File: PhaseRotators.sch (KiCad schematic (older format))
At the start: 7 parts, among them U2 74LVC1G00DCKR, U4 74LVC1G00DCKR, U8 74LCX574

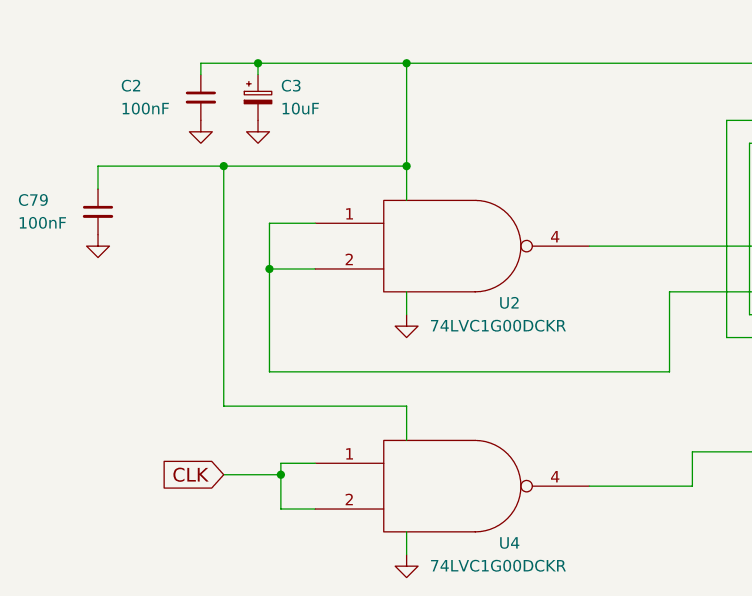
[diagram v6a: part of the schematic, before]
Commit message: PCB 74LCX574
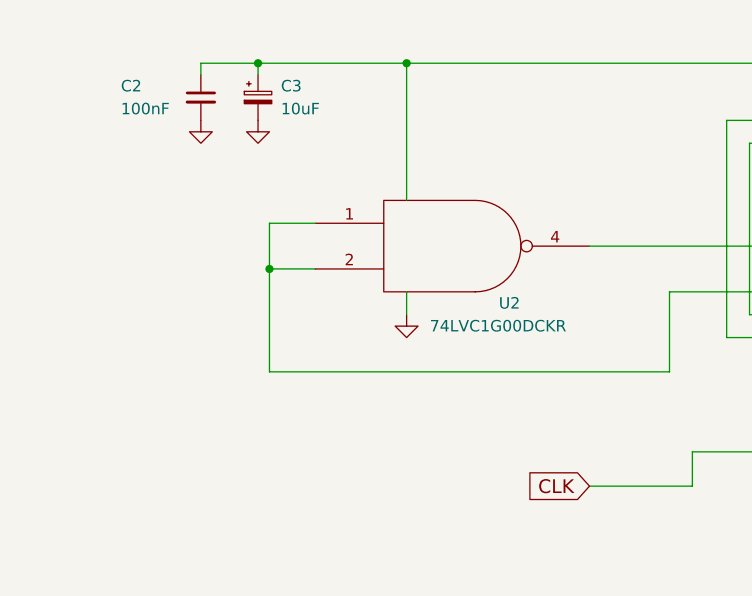
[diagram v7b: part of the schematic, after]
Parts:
- removed C79: 100nF, UI:C_1206_0603, symbol C_Small
- removed U4: 74LVC1G00DCKR, TO_SOT_Packages_SMD:SOT-353_SC-70-5, symbol 74LVC1G00DCKR
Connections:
- net CLK: now also U8.11 (Cp)
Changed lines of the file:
@@
 Comment4 ""
 $EndDescr
-Text GLabel 3600 3700 0    60   Input ~ 0
+Text GLabel 5200 3750 0    60   Input ~ 0
 CLK
 $Comp
@@
 $EndComp
 $Comp
-L GND #PWR43
+L GND #PWR42
 U 1 1 5EAC7395
 P 3750 2150
-F 0 "#PWR43" H 3750 1900 50  0001 C CNN
+F 0 "#PWR42" H 3750 1900 50  0001 C CNN
 F 1 "GND" H 3750 2000 50  0001 C CNN
 F 2 "" H 3750 2150 50  0001 C CNN
@@
 $EndComp
 $Comp
-L GND #PWR42
+L GND #PWR41
 U 1 1 5EAC76D0
 P 3500 2150
-F 0 "#PWR42" H 3500 1900 50  0001 C CNN
+F 0 "#PWR41" H 3500 1900 50  0001 C CNN
 F 1 "GND" H 3500 2000 50  0001 C CNN
 F 2 "" H 3500 2150 50  0001 C CNN
@@
 	6900 1900 6900 2650
 $Comp
-L GND #PWR46
+L GND #PWR44
 U 1 1 5ED0A7D2
 P 6900 3900
-F 0 "#PWR46" H 6900 3650 50  0001 C CNN
+F 0 "#PWR44" H 6900 3650 50  0001 C CNN
 F 1 "GND" H 6900 3750 50  0001 C CNN
 F 2 "" H 6900 3900 50  0001 C CNN
@@
 	4400 2900 4400 3000
 $Comp
-L GND #PWR44
+L GND #PWR43
 U 1 1 5ED0ABB8
 P 4400 3000
-F 0 "#PWR44" H 4400 2750 50  0001 C CNN
+F 0 "#PWR43" H 4400 2750 50  0001 C CNN
 F 1 "GND" H 4400 2850 50  0001 C CNN
 F 2 "" H 4400 3000 50  0001 C CNN
@@
 Wire Wire Line
 	5650 3600 6200 3600
-Wire Wire Line
-	3600 3700 3850 3700
-Wire Wire Line
-	3850 3650 3850 3850
-Wire Wire Line
-	3850 3650 4000 3650
-Wire Wire Line
-	3850 3850 4000 3850
-Connection ~ 3850 3700
 Connection ~ 4400 1900
 $Comp
@@
 	1    0    0    -1
 $EndComp
-$Comp
-L 74LVC1G00DCKR U4
-U 1 1 5ED1F8EE
-P 4600 3750
-F 0 "U4" H 4850 3500 50  0000 C CNN
-F 1 "74LVC1G00DCKR" H 4800 3400 50  0000 C CNN
-F 2 "TO_SOT_Packages_SMD:SOT-353_SC-70-5" H 4600 3750 50  0001 C CNN
-F 3 "" H 4600 3750 50  0001 C CNN
-	1    4600 3750
-	1    0    0    -1
-$EndComp
-Wire Wire Line
-	3050 2350 4400 2350
-Wire Wire Line
-	3600 3400 4400 3400
-Wire Wire Line
-	4400 3400 4400 3550
-Connection ~ 4400 2350
-$Comp
-L GND #PWR45
-U 1 1 5ED1F9E3
-P 4400 4050
-F 0 "#PWR45" H 4400 3800 50  0001 C CNN
-F 1 "GND" H 4400 3900 50  0001 C CNN
-F 2 "" H 4400 4050 50  0001 C CNN
-F 3 "" H 4400 4050 50  0001 C CNN
-	1    4400 4050
-	1    0    0    -1
-$EndComp
-Wire Wire Line
-	4400 3950 4400 4050
 Wire Wire Line
 	6100 3850 6900 3850
 Connection ~ 6100 3700
 Connection ~ 6900 3850
-$Comp
-L C_Small C79
-U 1 1 5ED21246
-P 3050 2550
-F 0 "C79" H 2700 2600 50  0000 L CNN
-F 1 "100nF" H 2700 2500 50  0000 L CNN
-F 2 "UI:C_1206_0603" H 3050 2550 50  0001 C CNN
-F 3 "" H 3050 2550 50  0001 C CNN
-	1    3050 2550
-	1    0    0    -1
-$EndComp
-$Comp
-L GND #PWR41
-U 1 1 5ED212C0
-P 3050 2650
-F 0 "#PWR41" H 3050 2400 50  0001 C CNN
-F 1 "GND" H 3050 2500 50  0001 C CNN
-F 2 "" H 3050 2650 50  0001 C CNN
-F 3 "" H 3050 2650 50  0001 C CNN
-	1    3050 2650
-	1    0    0    -1
-$EndComp
-Wire Wire Line
-	3050 2450 3050 2350
-Connection ~ 3600 2350
-Wire Wire Line
-	3600 2350 3600 3400
 $EndSCHEMATC

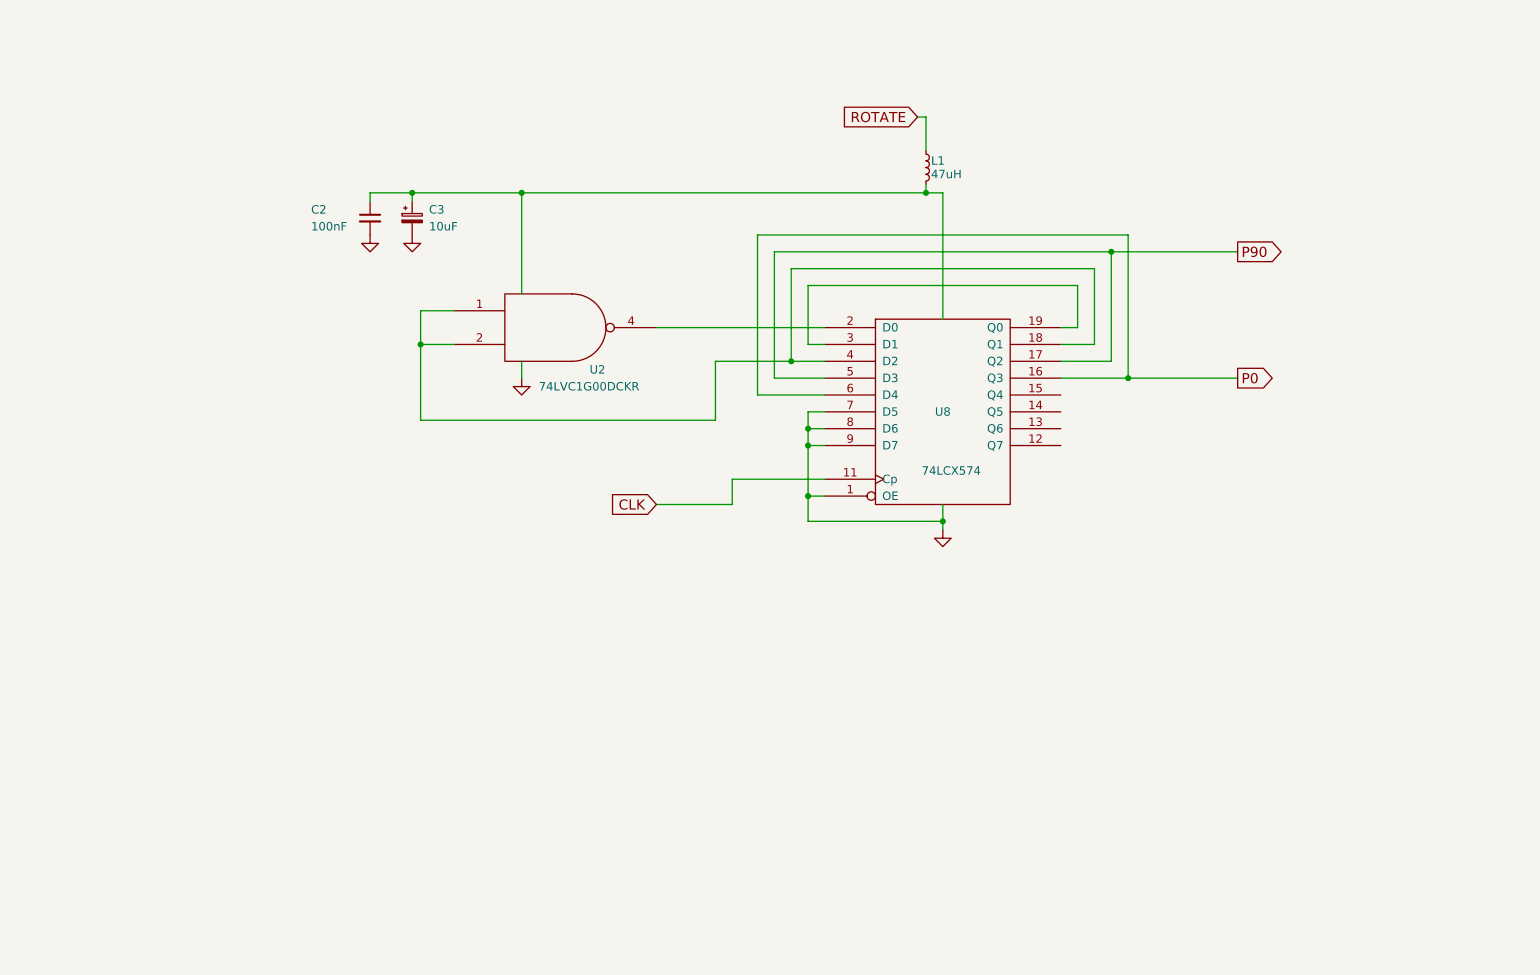
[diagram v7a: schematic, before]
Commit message: rotate phase with 74LVC74APW
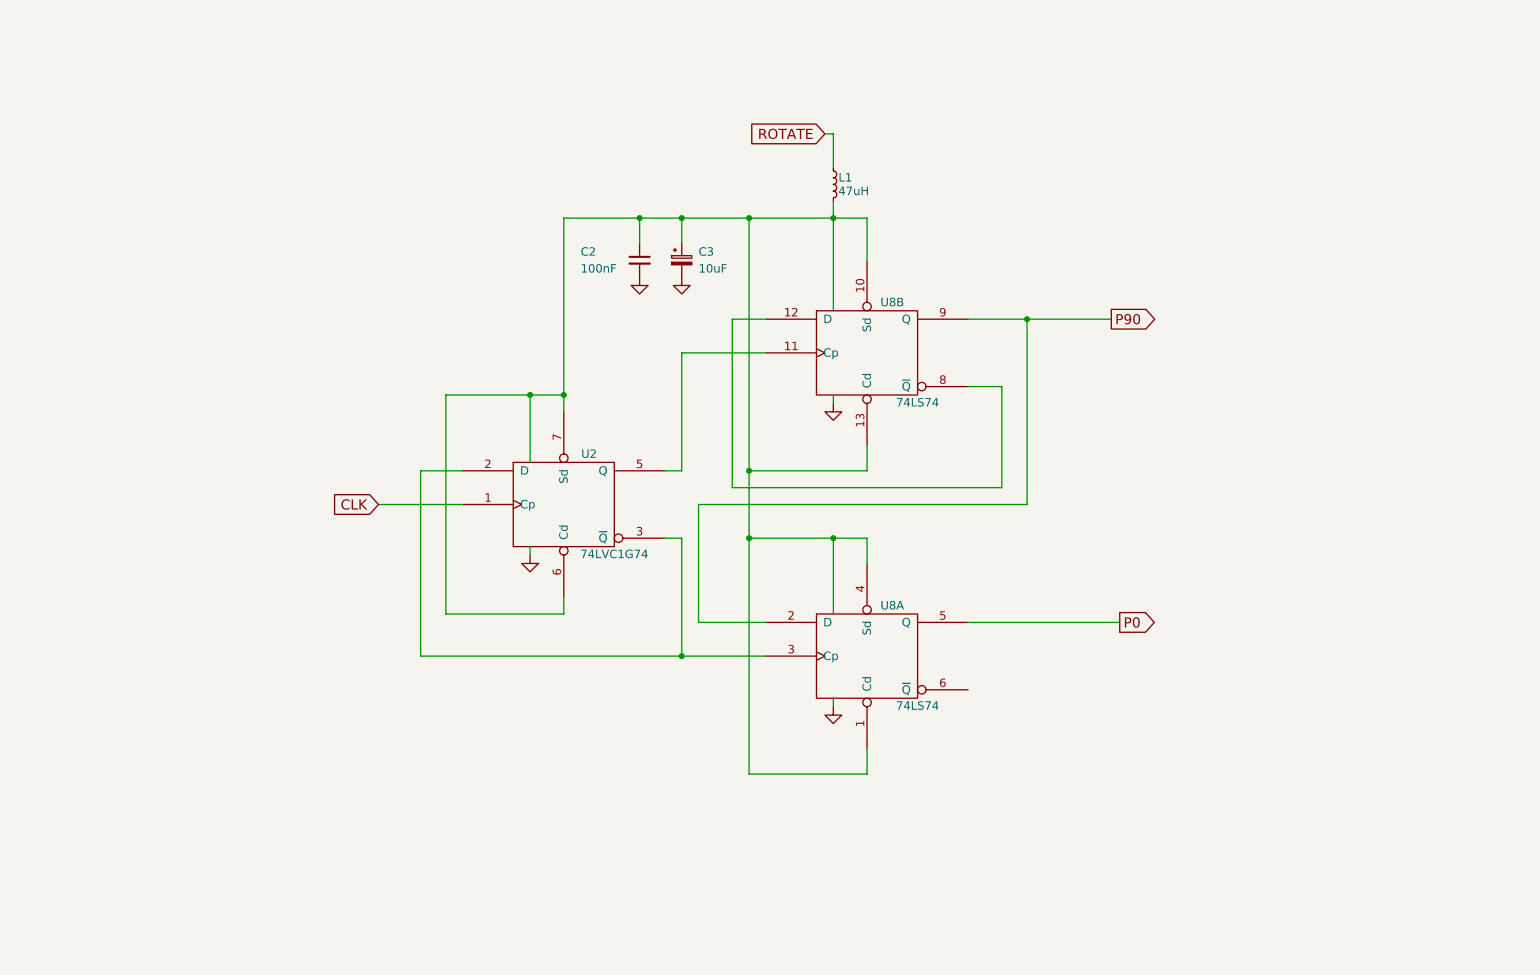
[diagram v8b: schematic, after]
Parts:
- removed U2: 74LVC1G00DCKR, TO_SOT_Packages_SMD:SOT-353_SC-70-5, symbol 74LVC1G00DCKR
- removed U8: 74LCX574, Housings_SSOP:TSSOP-20_4.4x6.5mm_Pitch0.65mm, symbol 74LS574
- added U2: 74LVC1G74, Housings_SSOP:TSSOP-8_3x3mm_Pitch0.65mm, symbol 74LVC1G74
- added U8: 74LS74, Housings_SSOP:TSSOP-14_4.4x5mm_Pitch0.65mm, symbol 74LS74
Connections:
- net CLK: now also U2.1 (Cp)
- net GND: now also U2.4 (GND), U8.7 (GND), U8.7 (GND)
- net P0: now also U8.5 (Q)
- net P90: now also U8.2 (D), U8.9 (Q)
- net VCC: now also U2.6 (Cd), U2.7 (Sd), U2.8 (VCC), U8.1 (Cd), U8.10 (Sd), U8.13 (Cd), U8.14 (VCC), U8.14 (VCC), U8.4 (Sd)
- new net: U2.2 (D), U2.3 (~Q), U8.3 (Cp)
- new net: U2.5 (Q), U8.11 (Cp)
- new net: U8.12 (D), U8.8 (~Q)
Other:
- moved on the sheet: C2, C3, L1
